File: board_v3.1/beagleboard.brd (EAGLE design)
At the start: 69.8 x 54.6 mm, 36 parts, among them U1 DWM1000

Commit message: board v3.1 beta 5: przepięte 2 TOF i MEN,M0,M1,M2, usunięte rezystory z tych linii, rerouting
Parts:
- removed R10, R11, R12, R13: 50k, rcl:R0603
- R16: value 100k -> 25k
- moved C6 36.2 mm to (45.4, 44.5), turned to 270 degrees
- moved C5 35.9 mm to (50.2, 44.5), turned to 270 degrees
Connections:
- net D4ECHO renamed AIN0
- removed net D4TRIG: U$1.83
- removed net N$104: U$1.79
- removed net N$16: U$1.77
- removed net N$18: U$1.4
- removed net N$20: U$1.12
- removed net N$21: U$1.6
- removed net N$22: U$1.16
- removed net N$23: U$1.37
- removed net N$24: R13.1, U$1.44
- removed net N$25: U$1.14
- removed net N$27: U$1.18
- removed net N$28: U$1.20
- removed net N$29: U$1.22
- removed net N$30: U$1.24
- removed net N$31: U$1.26
- removed net N$33: U$1.30
- removed net N$34: U$1.32
- removed net N$35: U$1.34
- removed net N$36: U$1.36
- removed net N$37: U$1.38
- removed net N$39: U$1.55
- removed net N$4: R10.2, U$1.41
- removed net N$40: U$1.75
- removed net N$41: U$1.57
- removed net N$42: U$1.76
- removed net N$43: U$1.74
- removed net N$51: U$1.27
- removed net N$53: U$1.59
- removed net N$54: U$1.61
- removed net N$55: U$1.71
- removed net N$56: U$1.29
- removed net N$57: U$1.31
- removed net N$58: U$1.33
- removed net N$59: U$1.35
- removed net N$62: U$1.56
- removed net N$63: U$1.58
- removed net N$64: U$1.60
- removed net N$65: U$1.62
- removed net N$7: R11.2, U$1.43
- removed net N$70: U$1.78
- removed net N$72: U$1.70
- removed net N$73: U$1.72
- removed net N$75: U$1.69
- removed net N$77: U$1.88
- removed net N$8: R12.1, U$1.42
- net M0: now also U$1.28; no longer R10.1
- net M1: now also U$1.29; no longer R13.2
- net M2: now also U$1.30; no longer R11.1
- net MEN: now also U$1.27; no longer R12.2
- net MLDIR: now also U$1.43; no longer U$1.40
- net MLSTEP: now also U$1.44; no longer U$1.39
- net TOF1: now also U$1.62; no longer U$1.7
- net TOF2: now also U$1.60; no longer U$1.8
- net TOF3: now also U$1.7; no longer U$1.9
- net TOF4: now also U$1.8; no longer U$1.10
- net TOF5: now also U$1.9; no longer U$1.28
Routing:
- net N$7: track 30.0 -> 0.00 mm
- net N$24: track 30.0 -> 0.00 mm
- net +12V: track 94.4 -> 69.1 mm
- net M2: track 25.8 -> 50.3 mm
- net N$8: track 24.1 -> 0.00 mm
- net N$4: track 24.1 -> 0.00 mm
- net M0: track 25.8 -> 45.2 mm
- net M1: track 25.8 -> 44.7 mm
- net TOF1: track 40.7 -> 23.8 mm
- net MEN: track 29.9 -> 43.7 mm
- net TOF5: track 10.4 -> 20.0 mm
- net MLDIR: track 69.9 -> 61.0 mm
- net TOF2: track 31.2 -> 37.2 mm
- net +3V3: track 171.5 -> 175.9 mm
- net MLSTEP: track 64.6 -> 61.0 mm
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
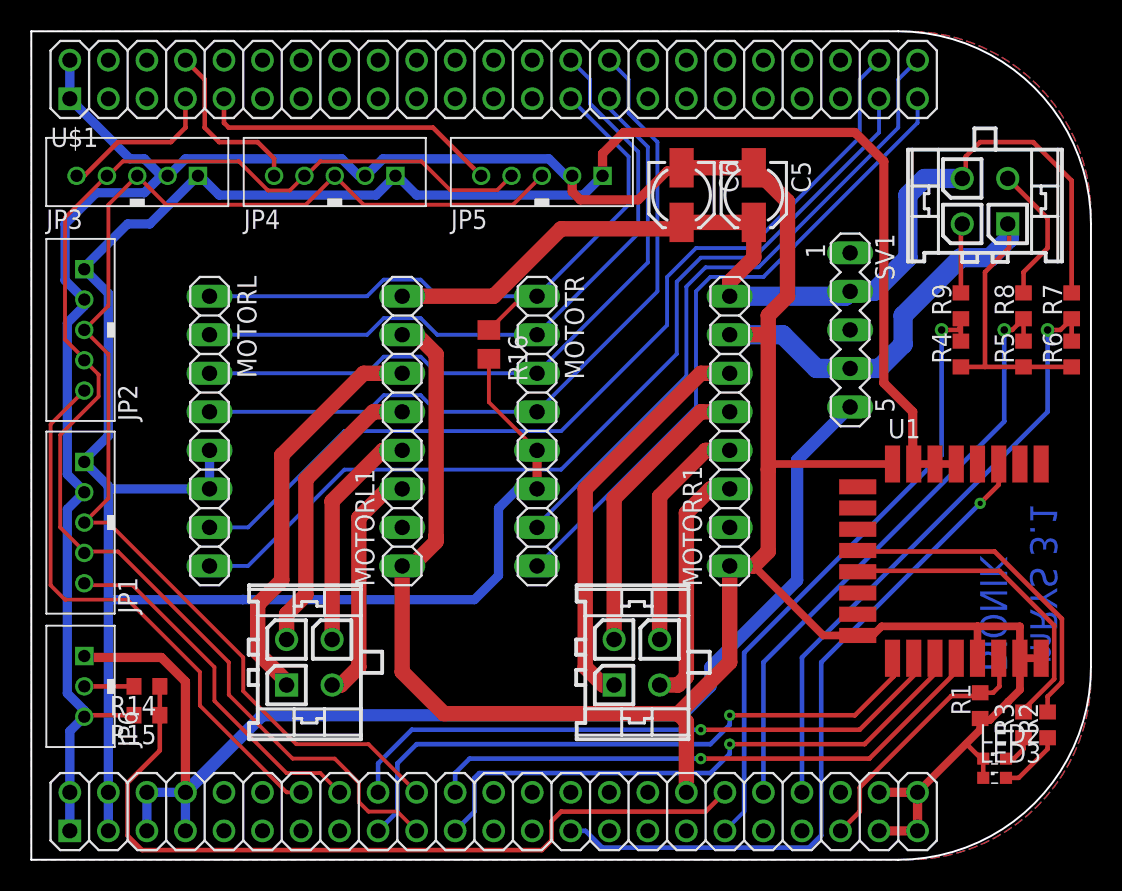
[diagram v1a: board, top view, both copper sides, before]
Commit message: board v3.1 beta 6: poprawione dzielniki napięcia baterii na płytce
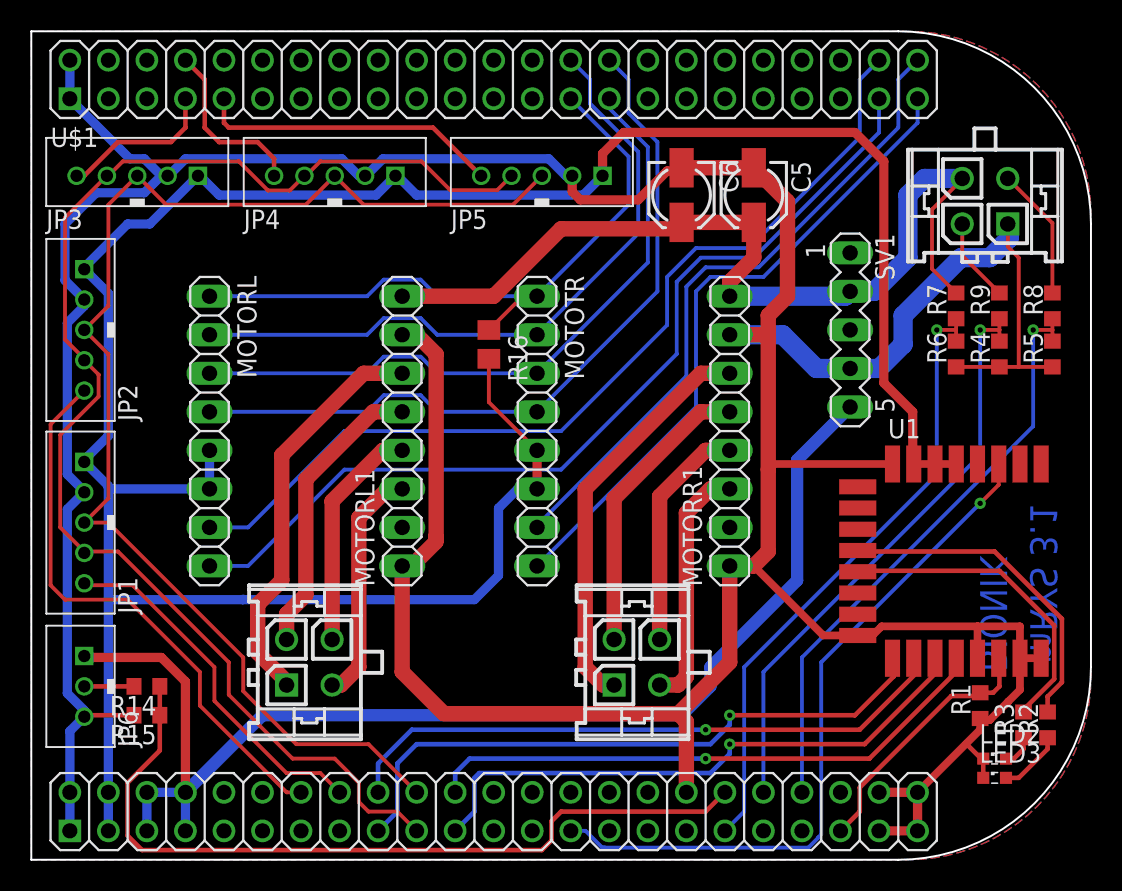
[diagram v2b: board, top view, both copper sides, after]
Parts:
- moved R6 7.62 mm to (63.5, 34.0)
- moved R7 7.62 mm to (63.5, 37.1)
- moved R4 2.54 mm to (66.4, 34.0)
- moved R9 2.54 mm to (66.4, 37.1)
- moved R5 1.91 mm to (69.8, 34.0)
- moved R8 1.91 mm to (69.8, 37.1)
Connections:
- removed net N$17: U$1.3
- removed net N$19: U$1.5
- removed net N$26: U$1.15
- removed net N$38: U$1.11
- removed net N$44: U$1.13
- removed net N$46: U$1.17
- removed net N$47: U$1.19
- removed net N$48: U$1.21
- removed net N$49: U$1.23
- removed net N$50: U$1.25
- net BAT_CELL1: now also U$1.84; no longer U$1.81
- net BAT_CELL2: now also U$1.86; no longer U$1.84
- net BAT_CELL3: now also U$1.81; no longer U$1.86
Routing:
- net +12V: track 69.1 -> 60.7 mm
- net BAT_CELL1: track 42.3 -> 39.1 mm
- net GND: track 299.2 -> 297.9 mm
- net BAT_CELL3: track 40.6 -> 41.6 mm
- net 3V5: track 4.58 -> 5.56 mm
- net BAT_CELL2: track 40.1 -> 39.5 mm
- net 7V: track 9.29 -> 8.77 mm
